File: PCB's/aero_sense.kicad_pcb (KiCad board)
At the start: 2 copper layers, 58 x 58 mm, 9 parts, among them J1 10164228-0201A1RLF, J2 10164228-0201A1RLF, J3 10164228-0201A1RLF, J4 10164228-0201A1RLF, U1 STM32F415ZGT6, U2 SHT45-AD1F-R2, U3 SGP41-D-R4, U4 MS560702BA03-00, U5 ICM-42688-P

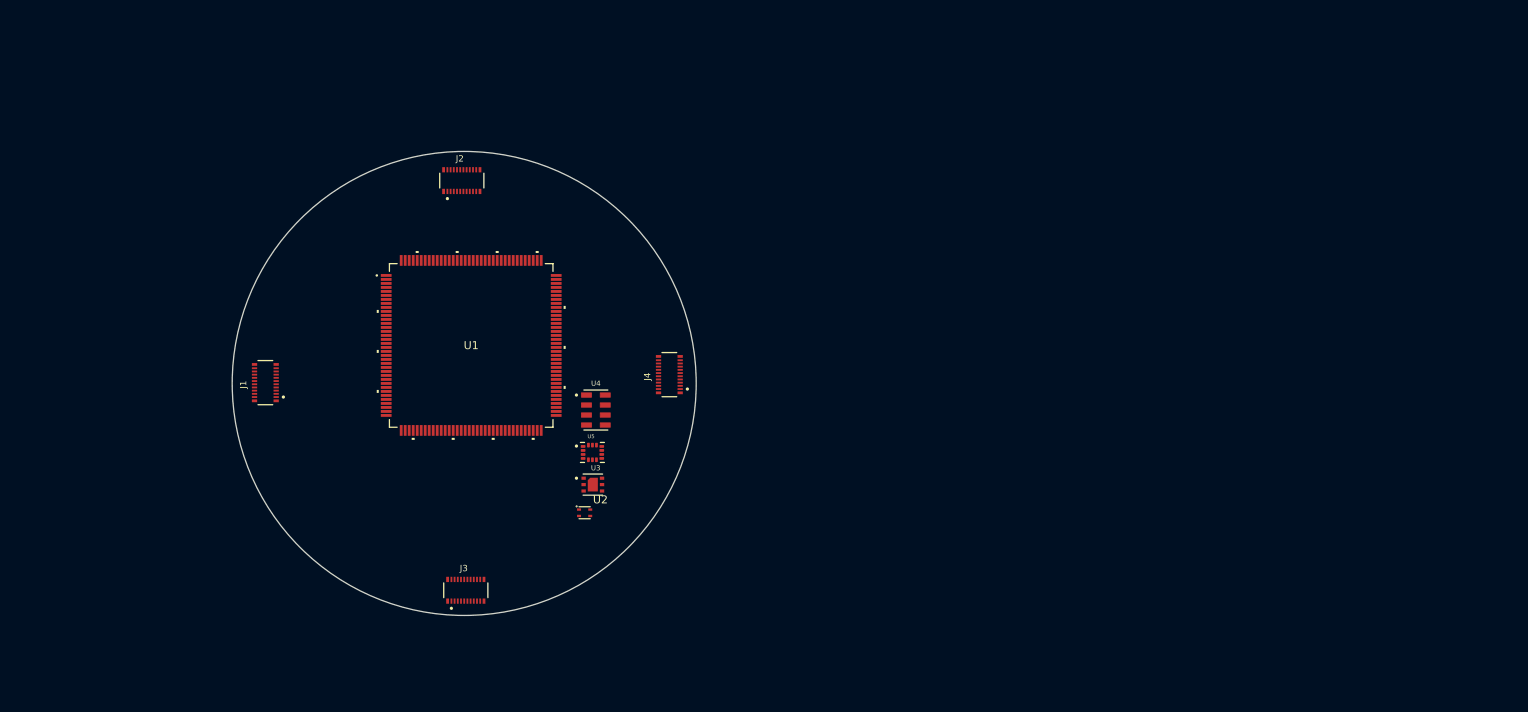
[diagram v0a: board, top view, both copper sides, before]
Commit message: power schematic finalized, changed mcu and added eMMC,  other changes in the schematic, reorganized schematics
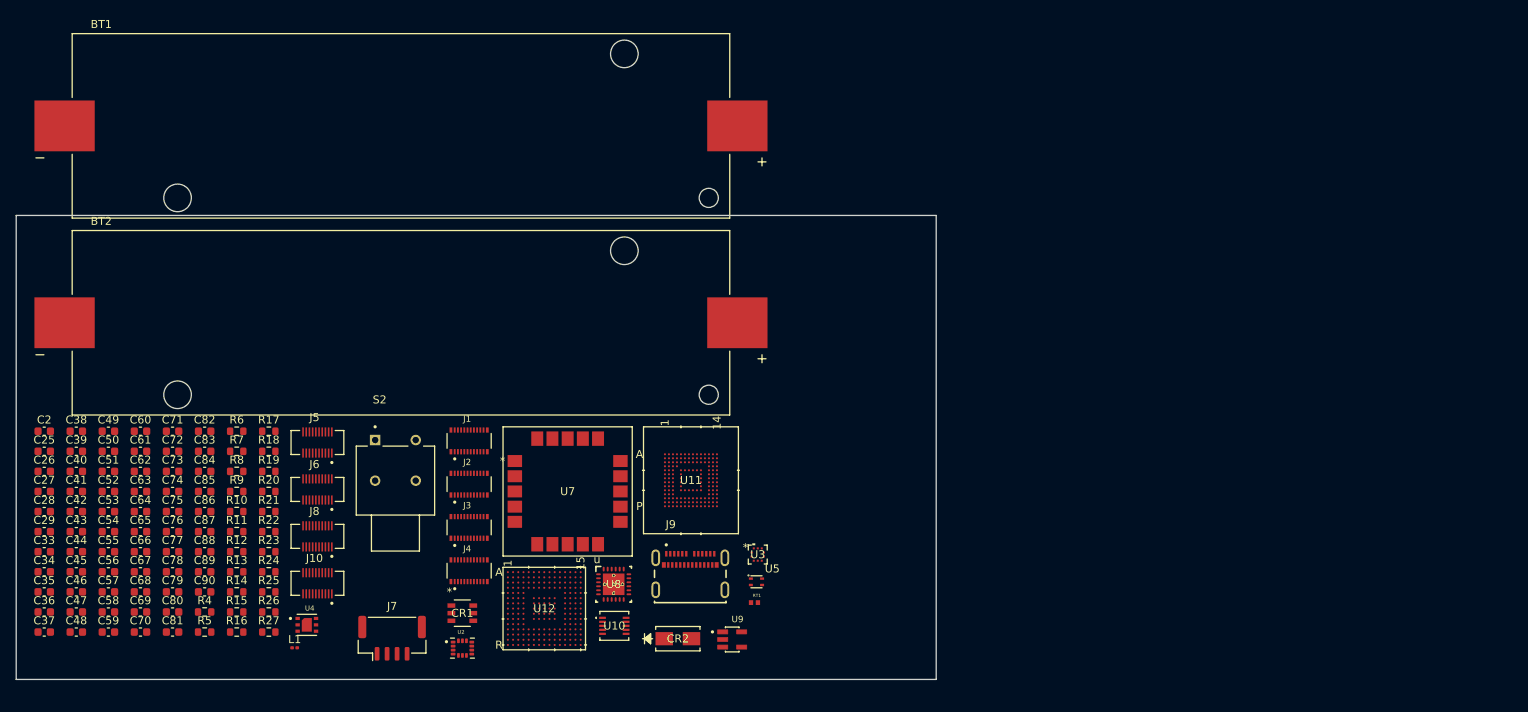
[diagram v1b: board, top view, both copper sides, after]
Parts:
- removed U1: STM32F415ZGT6, MyComponents:LQFP144-20x20mm
- added BT1: 1122, MyComponents:BAT_1122, F.Cu at (110.1, 57.3)
- added BT2: 1122, MyComponents:BAT_1122, F.Cu at (110.1, 81.9)
- added C2: 100Nf, Capacitor_SMD:C_0603_1608Metric, F.Cu at (65.5, 95.5)
- added C25: 100nF, Capacitor_SMD:C_0603_1608Metric, F.Cu at (65.5, 98.0)
- added C26: 100nF, Capacitor_SMD:C_0603_1608Metric, F.Cu at (65.5, 100.5)
- added C27: 100nF, Capacitor_SMD:C_0603_1608Metric, F.Cu at (65.5, 103.0)
- added C28: 1uF, Capacitor_SMD:C_0603_1608Metric, F.Cu at (65.5, 105.5)
- added C29: 1uF, Capacitor_SMD:C_0603_1608Metric, F.Cu at (65.5, 108.0)
- added C33: 1uF, Capacitor_SMD:C_0603_1608Metric, F.Cu at (65.5, 110.5)
- added C34: 100nF, Capacitor_SMD:C_0603_1608Metric, F.Cu at (65.5, 113.0)
- added C35: 100nF, Capacitor_SMD:C_0603_1608Metric, F.Cu at (65.5, 115.6)
- added C36: 100nF, Capacitor_SMD:C_0603_1608Metric, F.Cu at (65.5, 118.1)
- added C37: 100nF, Capacitor_SMD:C_0603_1608Metric, F.Cu at (65.5, 120.6)
- added C38: 100nF, Capacitor_SMD:C_0603_1608Metric, F.Cu at (69.5, 95.5)
- added C39: 100nF, Capacitor_SMD:C_0603_1608Metric, F.Cu at (69.5, 98.0)
- added C40: 100nF, Capacitor_SMD:C_0603_1608Metric, F.Cu at (69.5, 100.5)
- added C41: 100nF, Capacitor_SMD:C_0603_1608Metric, F.Cu at (69.5, 103.0)
- added C42: 1uF, Capacitor_SMD:C_0603_1608Metric, F.Cu at (69.5, 105.5)
- added C43: 100nF, Capacitor_SMD:C_0603_1608Metric, F.Cu at (69.5, 108.0)
- added C44: 100nF, Capacitor_SMD:C_0603_1608Metric, F.Cu at (69.5, 110.5)
- added C45: 100nF, Capacitor_SMD:C_0603_1608Metric, F.Cu at (69.5, 113.0)
- added C46: 100nF, Capacitor_SMD:C_0603_1608Metric, F.Cu at (69.5, 115.6)
- added C47: 100nF, Capacitor_SMD:C_0603_1608Metric, F.Cu at (69.5, 118.1)
- added C48: 100nF, Capacitor_SMD:C_0603_1608Metric, F.Cu at (69.5, 120.6)
- added C49: 100nF, Capacitor_SMD:C_0603_1608Metric, F.Cu at (73.5, 95.5)
- added C50: 100nF, Capacitor_SMD:C_0603_1608Metric, F.Cu at (73.5, 98.0)
- added C51: 100nF, Capacitor_SMD:C_0603_1608Metric, F.Cu at (73.5, 100.5)
- added C52: 100nF, Capacitor_SMD:C_0603_1608Metric, F.Cu at (73.5, 103.0)
- added C53: 100nF, Capacitor_SMD:C_0603_1608Metric, F.Cu at (73.5, 105.5)
- added C54: 100nF, Capacitor_SMD:C_0603_1608Metric, F.Cu at (73.5, 108.0)
- added C55: 100nF, Capacitor_SMD:C_0603_1608Metric, F.Cu at (73.5, 110.5)
- added C56: 4.7uF, Capacitor_SMD:C_0603_1608Metric, F.Cu at (73.5, 113.0)
- added C57: 100nF, Capacitor_SMD:C_0603_1608Metric, F.Cu at (73.5, 115.6)
- added C58: 4.7uF, Capacitor_SMD:C_0603_1608Metric, F.Cu at (73.5, 118.1)
- added C59: 100nF, Capacitor_SMD:C_0603_1608Metric, F.Cu at (73.5, 120.6)
- added C60: 10uF, Capacitor_SMD:C_0603_1608Metric, F.Cu at (77.5, 95.5)
- added C61: 1uF, Capacitor_SMD:C_0603_1608Metric, F.Cu at (77.5, 98.0)
- added C62: 47nF, Capacitor_SMD:C_0603_1608Metric, F.Cu at (77.5, 100.5)
- added C63: 10uF, Capacitor_SMD:C_0603_1608Metric, F.Cu at (77.5, 103.0)
- added C64: 10uF, Capacitor_SMD:C_0603_1608Metric, F.Cu at (77.5, 105.5)
- added C65: 4.7uF, Capacitor_SMD:C_0603_1608Metric, F.Cu at (77.5, 108.0)
- added C66: 40uF, Capacitor_SMD:C_0603_1608Metric, F.Cu at (77.5, 110.5)
- added C67: 10uF, Capacitor_SMD:C_0603_1608Metric, F.Cu at (77.5, 113.0)
- added C68: 10uF, Capacitor_SMD:C_0603_1608Metric, F.Cu at (77.5, 115.6)
- added C69: 10uF, Capacitor_SMD:C_0603_1608Metric, F.Cu at (77.5, 118.1)
- added C70: 10uF, Capacitor_SMD:C_0603_1608Metric, F.Cu at (77.5, 120.6)
- added C71: 10uF, Capacitor_SMD:C_0603_1608Metric, F.Cu at (81.5, 95.5)
- added C72: 1uF, Capacitor_SMD:C_0603_1608Metric, F.Cu at (81.5, 98.0)
- added C73: 100nF, Capacitor_SMD:C_0603_1608Metric, F.Cu at (81.5, 100.5)
- added C74: 100nF, Capacitor_SMD:C_0603_1608Metric, F.Cu at (81.5, 103.0)
- added C75: 100nF, Capacitor_SMD:C_0603_1608Metric, F.Cu at (81.5, 105.5)
- added C76: 100nF, Capacitor_SMD:C_0603_1608Metric, F.Cu at (81.5, 108.0)
- added C77: 100nF, Capacitor_SMD:C_0603_1608Metric, F.Cu at (81.5, 110.5)
- added C78: 100nF, Capacitor_SMD:C_0603_1608Metric, F.Cu at (81.5, 113.0)
- added C79: 100nF, Capacitor_SMD:C_0603_1608Metric, F.Cu at (81.5, 115.6)
- added C80: 100nF, Capacitor_SMD:C_0603_1608Metric, F.Cu at (81.5, 118.1)
- added C81: 4.7uF, Capacitor_SMD:C_0603_1608Metric, F.Cu at (81.5, 120.6)
- added C82: 100nF, Capacitor_SMD:C_0603_1608Metric, F.Cu at (85.6, 95.5)
- added C83: 2.2uF, Capacitor_SMD:C_0603_1608Metric, F.Cu at (85.6, 98.0)
- added C84: 100nF, Capacitor_SMD:C_0603_1608Metric, F.Cu at (85.6, 100.5)
- added C85: 100nF, Capacitor_SMD:C_0603_1608Metric, F.Cu at (85.6, 103.0)
- added C86: 10nF, Capacitor_SMD:C_0603_1608Metric, F.Cu at (85.6, 105.5)
- added C87: 100nF, Capacitor_SMD:C_0603_1608Metric, F.Cu at (85.6, 108.0)
- added C88: 100nF, Capacitor_SMD:C_0603_1608Metric, F.Cu at (85.6, 110.5)
- added C89: 2uF, Capacitor_SMD:C_0603_1608Metric, F.Cu at (85.6, 113.0)
- added C90: 2uF, Capacitor_SMD:C_0603_1608Metric, F.Cu at (85.6, 115.6)
- added CR1: USBLC6-2SC6, MyComponents:SOT23-6L_STM, F.Cu at (117.8, 118.2)
- added CR2: SMAJ12A, MyComponents:SMASeries_LTF, F.Cu at (144.7, 121.4)
- added J10: 10164227-0205A1RLF, MyComponents:AMPHENOL_10164227-0205A1RLF, F.Cu at (99.7, 114.5)
- added J5: 10164227-0205A1RLF, MyComponents:AMPHENOL_10164227-0205A1RLF, F.Cu at (99.7, 96.9)
- added J6: 10164227-0205A1RLF, MyComponents:AMPHENOL_10164227-0205A1RLF, F.Cu at (99.7, 102.8)
- added J7: Conn_01x04_Pin, Connector_JST:JST_GH_BM04B-GHS-TBT_1x04-1MP_P1.25mm_Vertical, F.Cu at (109.0, 121.3)
- added J8: 10164227-0205A1RLF, MyComponents:AMPHENOL_10164227-0205A1RLF, F.Cu at (99.7, 108.6)
- added J9: USB4081-03-A_REV0.1, MyComponents:GCT_USB4081-03-A_REV0.1, F.Cu at (146.3, 111.3)
- added L1: 2uH, Inductor_SMD:L_0201_0603Metric, F.Cu at (96.8, 122.5)
- added R10: 0R, Resistor_SMD:R_0603_1608Metric, F.Cu at (89.6, 105.5)
- added R11: 10kR, Resistor_SMD:R_0603_1608Metric, F.Cu at (89.6, 108.0)
- added R12: 10kR, Resistor_SMD:R_0603_1608Metric, F.Cu at (89.6, 110.5)
- added R13: 10kR, Resistor_SMD:R_0603_1608Metric, F.Cu at (89.6, 113.0)
- added R14: 260R, Resistor_SMD:R_0603_1608Metric, F.Cu at (89.6, 115.6)
- added R15: 10kR, Resistor_SMD:R_0603_1608Metric, F.Cu at (89.6, 118.1)
- added R16: 10kR, Resistor_SMD:R_0603_1608Metric, F.Cu at (89.6, 120.6)
- added R17: 10kR, Resistor_SMD:R_0603_1608Metric, F.Cu at (93.6, 95.5)
- added R18: 3.3kR, Resistor_SMD:R_0603_1608Metric, F.Cu at (93.6, 98.0)
- added R19: 5.1kR, Resistor_SMD:R_0603_1608Metric, F.Cu at (93.6, 100.5)
- added R20: 5.1kR, Resistor_SMD:R_0603_1608Metric, F.Cu at (93.6, 103.0)
- added R21: 10kR, Resistor_SMD:R_0603_1608Metric, F.Cu at (93.6, 105.5)
- added R22: 22R, Resistor_SMD:R_0603_1608Metric, F.Cu at (93.6, 108.0)
- added R23: 22R, Resistor_SMD:R_0603_1608Metric, F.Cu at (93.6, 110.5)
- added R24: 10kR, Resistor_SMD:R_0603_1608Metric, F.Cu at (93.6, 113.0)
- added R25: 10kR, Resistor_SMD:R_0603_1608Metric, F.Cu at (93.6, 115.6)
- added R26: 0R, Resistor_SMD:R_0603_1608Metric, F.Cu at (93.6, 118.1)
- added R27: R, Resistor_SMD:R_0603_1608Metric, F.Cu at (93.6, 120.6)
- added R4: 10kR, Resistor_SMD:R_0603_1608Metric, F.Cu at (85.6, 118.1)
- added R5: 10R, Resistor_SMD:R_0603_1608Metric, F.Cu at (85.6, 120.6)
- added R6: 10, Resistor_SMD:R_0603_1608Metric, F.Cu at (89.6, 95.5)
- added R7: 10kR, Resistor_SMD:R_0603_1608Metric, F.Cu at (89.6, 98.0)
- added R8: 10kR, Resistor_SMD:R_0603_1608Metric, F.Cu at (89.6, 100.5)
- added R9: 4.7R, Resistor_SMD:R_0603_1608Metric, F.Cu at (89.6, 103.0)
- added RT1: NCP15XH103F03RC, MyComponents:THRMC1005X55N, F.Cu at (154.3, 116.9)
- added S2: AB11AH-HC, MyComponents:SW_AB11AH-HC, F.Cu at (109.4, 101.6)
- added U10: TS3USB221DRCR, MyComponents:DRC10_2P4X1P65, F.Cu at (136.8, 119.8)
- added U11: KLM8G1GETF-B041, MyComponents:KLMBG2JENB-B041_SAM, F.Cu at (146.3, 101.6)
- added U12: STM32F417IGH6, MyComponents:BGA 176, F.Cu at (128.0, 117.6)
- added U7: SAM-M10Q-00B, MyComponents:SAM-M10Q_UBL, F.Cu at (130.9, 103.0)
- added U8: BQ25895RTWR, MyComponents:RTW0024H, F.Cu at (136.7, 114.6)
- added U9: AP2112K-3.3TRG1, MyComponents:SOT95P285X140-5N, F.Cu at (151.5, 121.5)
- U2: value SHT45-AD1F-R2 -> ICM-42688-P; footprint MyComponents:SHT4X -> MyComponents:PQFN50P300X250X97-14N
- U3: value SGP41-D-R4 -> BMP581; footprint MyComponents:XDCR_SGP41-D-R4 -> MyComponents:QFN10_BMP581_BOS
- U4: value MS560702BA03-00 -> SGP41-D-R4; footprint MyComponents:SON125P500X300X100-8N -> MyComponents:XDCR_SGP41-D-R4
- U5: value ICM-42688-P -> SHT45-AD1F-R2; footprint MyComponents:PQFN50P300X250X97-14N -> MyComponents:SHT4X
- moved U4 45.0 mm to (98.3, 119.7)
- moved J2 38.0 mm to (118.6, 102.1)
- moved J4 35.0 mm to (118.6, 112.9), turned to 0 degrees
- moved J1 26.5 mm to (118.6, 96.7), turned to 0 degrees
- moved U5 26.1 mm to (154.5, 114.3)
- moved U2 22.8 mm to (117.8, 122.6)
- moved U3 22.4 mm to (154.7, 110.9)
- moved J3 7.87 mm to (118.6, 107.5)
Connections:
- J2 pad 1: unconnected-(J2-Pad1) -> GND
- J2 pad 10: unconnected-(J2-Pad10) -> VBAT
- J2 pad 11: unconnected-(J2-Pad11) -> VBAT
- J2 pad 12: unconnected-(J2-Pad12) -> VBAT
- J2 pad 13: unconnected-(J2-Pad13) -> VBAT
- J2 pad 14: unconnected-(J2-Pad14) -> VBAT
- J2 pad 15: unconnected-(J2-Pad15) -> VBAT
- J2 pad 16: unconnected-(J2-Pad16) -> VBAT
- J2 pad 17: unconnected-(J2-Pad17) -> GND
- J2 pad 18: unconnected-(J2-Pad18) -> GND
- J2 pad 19: unconnected-(J2-Pad19) -> GND
- J2 pad 2: unconnected-(J2-Pad2) -> GND
- J2 pad 20: unconnected-(J2-Pad20) -> GND
- J2 pad 3: unconnected-(J2-Pad3) -> GND
- J2 pad 4: unconnected-(J2-Pad4) -> GND
- J2 pad 5: unconnected-(J2-Pad5) -> VBAT
- J2 pad 6: unconnected-(J2-Pad6) -> VBAT
- J2 pad 7: unconnected-(J2-Pad7) -> VBAT
- J2 pad 8: unconnected-(J2-Pad8) -> VBAT
- J2 pad 9: unconnected-(J2-Pad9) -> VBAT
- J3 pad 1: unconnected-(J3-Pad1) -> GND
- J3 pad 10: unconnected-(J3-Pad10) -> I2C1_SDA
- J3 pad 11: unconnected-(J3-Pad11) -> VBAT
- J3 pad 12: unconnected-(J3-Pad12) -> I2C1_SCL
- J3 pad 13: unconnected-(J3-Pad13) -> VBAT
- J3 pad 14: unconnected-(J3-Pad14) -> GND
- J3 pad 15: unconnected-(J3-Pad15) -> VBAT
- J3 pad 16: unconnected-(J3-Pad16) -> GND
- J3 pad 17: unconnected-(J3-Pad17) -> VBAT
- J3 pad 18: unconnected-(J3-Pad18) -> GND
- J3 pad 19: unconnected-(J3-Pad19) -> GND
- J3 pad 2: unconnected-(J3-Pad2) -> GND
- J3 pad 20: unconnected-(J3-Pad20) -> GND
- J3 pad 3: unconnected-(J3-Pad3) -> VBAT
- J3 pad 4: unconnected-(J3-Pad4) -> GND
- J3 pad 5: unconnected-(J3-Pad5) -> VBAT
- J3 pad 6: unconnected-(J3-Pad6) -> GND
- J3 pad 7: unconnected-(J3-Pad7) -> VBAT
- J3 pad 8: unconnected-(J3-Pad8) -> GND
- J3 pad 9: unconnected-(J3-Pad9) -> VBAT
- U2 pad 1: unconnected-(U2-SDA-Pad1) -> SPI1_MISO
- U2 pad 2: unconnected-(U2-SCL-Pad2) -> GND
- U2 pad 3: unconnected-(U2-VDD-Pad3) -> GND
- U2 pad 4: unconnected-(U2-VSS-Pad4) -> 42688_INT1
- U3 pad 1: unconnected-(U3-VDD-Pad1) -> Net-(U3-VDDIO)
- U3 pad 2: unconnected-(U3-VSS-Pad2) -> I2C1_SCL
- U3 pad 3: unconnected-(U3-SDA-Pad3) -> GND
- U3 pad 4: unconnected-(U3-N/A-Pad4) -> I2C1_SDA
- U3 pad 5: unconnected-(U3-VDDH-Pad5) -> GND
- U3 pad 6: unconnected-(U3-SCL-Pad6) -> VBAT
- U4 pad 1: unconnected-(U4-VDD-Pad1) -> Net-(U4-VDD)
- U4 pad 2: unconnected-(U4-PS-Pad2) -> GND
- U4 pad 3: unconnected-(U4-GND-Pad3) -> I2C1_SDA
- U4 pad 4: Net-(U4-~{CSB}-Pad4) -> GND
- U4 pad 5: Net-(U4-~{CSB}-Pad4) -> VBAT
- U4 pad 6: unconnected-(U4-SDO-Pad6) -> I2C1_SCL
- U4 pad 7: unconnected-(U4-SDI/SDA-Pad7) -> GND
- U5 pad 1: unconnected-(U5-AP_SDO/AP_AD0-Pad1) -> I2C1_SDA
- U5 pad 2: unconnected-(U5-RESV_2-Pad2) -> I2C1_SCL
- U5 pad 3: unconnected-(U5-RESV_3-Pad3) -> VBAT
- U5 pad 4: unconnected-(U5-INT1/INT-Pad4) -> GND
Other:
- board size 58 x 58 mm -> 115 x 58 mm

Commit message: unfinished changes
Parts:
- C2, C25, C26, C27, C28, C29, C33, C34, C35, C36, C37, C38, C39, C40, C41, C42, C43, C44, C45, C46, C47, C48, C49, C50, C51, C52, C53, C54, C55, C56, C57, C58, C59, C60, C61, C62, C63, C64, C65, C66, C67, C68, C69, C70, C71, C72, C73, C74, C75, C76, C77, C78, C79, C80, C81, C82, C83, C84, C85, C86, C87, C88, C89, C90, R10, R11, R12, R13, R14, R15, R16, R17, R18, R19, R20, R21, R22, R23, R24, R25, R26, R27, R4, R5, R6, R7, R8, R9: moved to B.Cu
- moved C2 170.0 mm to (235.3, 87.0), turned to 180 degrees
- moved C25 170.0 mm to (235.3, 89.5), turned to 180 degrees
- moved C26 170.0 mm to (235.3, 92.0), turned to 180 degrees
- moved C27 170.0 mm to (235.3, 94.5), turned to 180 degrees
- moved C28 170.0 mm to (235.3, 97.0), turned to 180 degrees
- moved C29 170.0 mm to (235.3, 99.5), turned to 180 degrees
- moved C33 170.0 mm to (235.3, 102.0), turned to 180 degrees
- moved C34 170.0 mm to (235.3, 104.5), turned to 180 degrees
- moved C35 170.0 mm to (235.3, 107.0), turned to 180 degrees
- moved C36 170.0 mm to (235.3, 109.5), turned to 180 degrees
- moved C37 170.0 mm to (235.3, 112.1), turned to 180 degrees
- moved C38 162.0 mm to (231.2, 87.0), turned to 180 degrees
- moved C39 162.0 mm to (231.2, 89.5), turned to 180 degrees
- moved C40 162.0 mm to (231.2, 92.0), turned to 180 degrees
- moved C41 162.0 mm to (231.2, 94.5), turned to 180 degrees
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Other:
- board size 115 x 58 mm -> 58 x 58 mm
